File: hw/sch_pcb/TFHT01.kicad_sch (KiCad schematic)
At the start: 30 parts, among them J1 SM04B-GHS-TB, J2 SM04B-GHS-TB, M1 M3, M2 M3, M3 M3, M4 M3, M5 M3, M6 M3, M7 CAP-SF2, Q1 BC817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

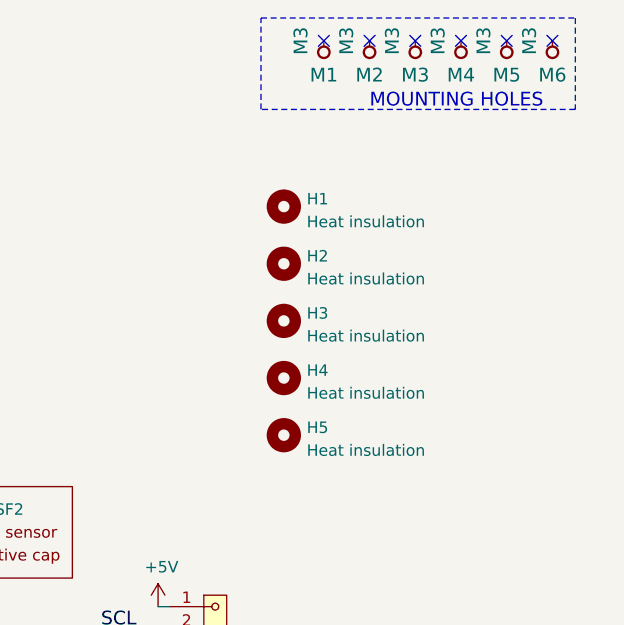
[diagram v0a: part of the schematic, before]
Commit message: Uprava PCB a kontrola pred vyrobou
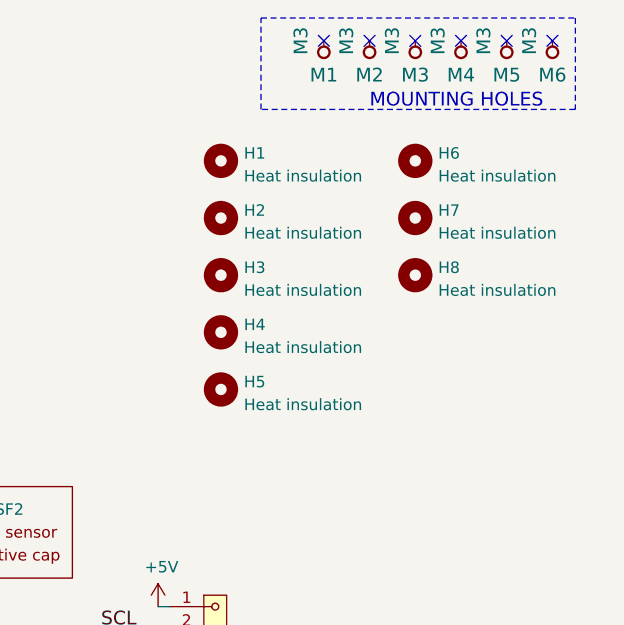
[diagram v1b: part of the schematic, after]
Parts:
- added H6, H7, H8: Heat insulation, Mlab_Mechanical:MountingHole_1mm, symbol Mechanical:MountingHole
- H2: footprint MountingHole:MountingHole_2mm -> Mlab_Mechanical:MountingHole_1mm
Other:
- moved on the sheet: H1, H2, H3, H4, H5

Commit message: Edit UST_ID
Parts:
- U1: UST_ID 5c70984612875079b91f89e4 -> 65103c42462c6d9e72054b8e
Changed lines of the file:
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@@
       (effects (font (size 1.27 1.27)) hide)
     )
-    (property "UST_ID" "5c70984612875079b91f89e4" (at 128.27 97.79 0)
+    (property "UST_ID" "65103c42462c6d9e72054b8e" (at 128.27 97.79 0)
       (effects (font (size 1.27 1.27)) hide)
     )

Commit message: Edit ID
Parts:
- R2: UST_ID 5c70984512875079b91f8956 -> 5c70984512875079b91f8962
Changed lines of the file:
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@@
       (effects (font (size 1.27 1.27)) hide)
     )
-    (property "UST_ID" "5c70984512875079b91f8956" (at 183.515 127 0)
+    (property "UST_ID" "5c70984512875079b91f8962" (at 183.515 127 0)
       (effects (font (size 1.27 1.27)) hide)
     )
